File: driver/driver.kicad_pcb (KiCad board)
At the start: 2 copper layers, 100 x 100 mm, 104 parts, among them J1 OUT_A, J2 OUT_B, J3 UART_DEBUG, J4 USB_B_Micro, J5 CH340E module, J6 1602 I2C LCD, J7 IN_VCC, J8 IN_GND, J9 SWD, Q1 TPHR6503PL, Q2 TPHR6503PL, Q3 TPHR6503PL, Q4 TPHR6503PL, SW1 SW_Push, SW2 SW_Push, U1 MT3608, U10 PC817, U2 AMS1117-5.0, U3 AMS1117-3.3, U4 TC4427, U5 TC4427, U6 STM32F103C8Tx, U7 INA226, U8 MCP9804_MSOP, U9 PC817, Y1 8MHz

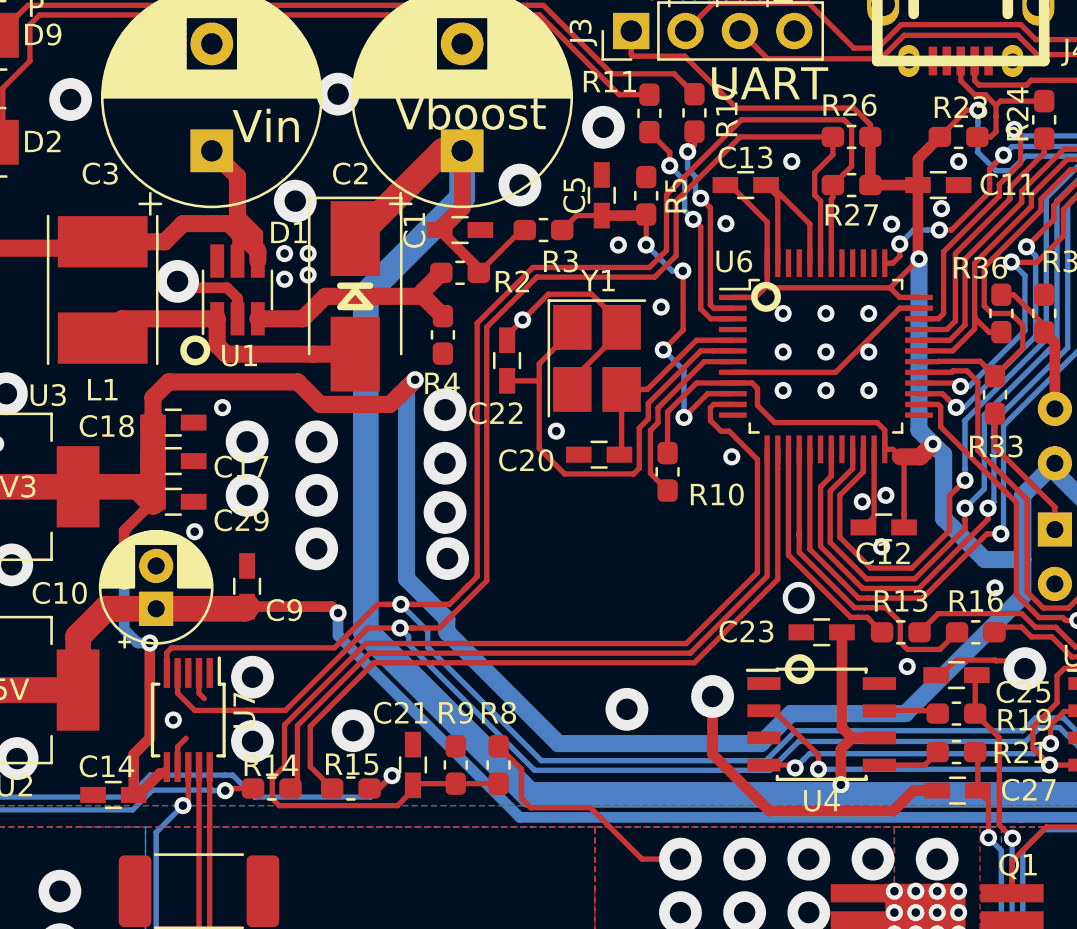
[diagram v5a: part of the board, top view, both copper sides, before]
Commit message: driver: Fatten a few power traces
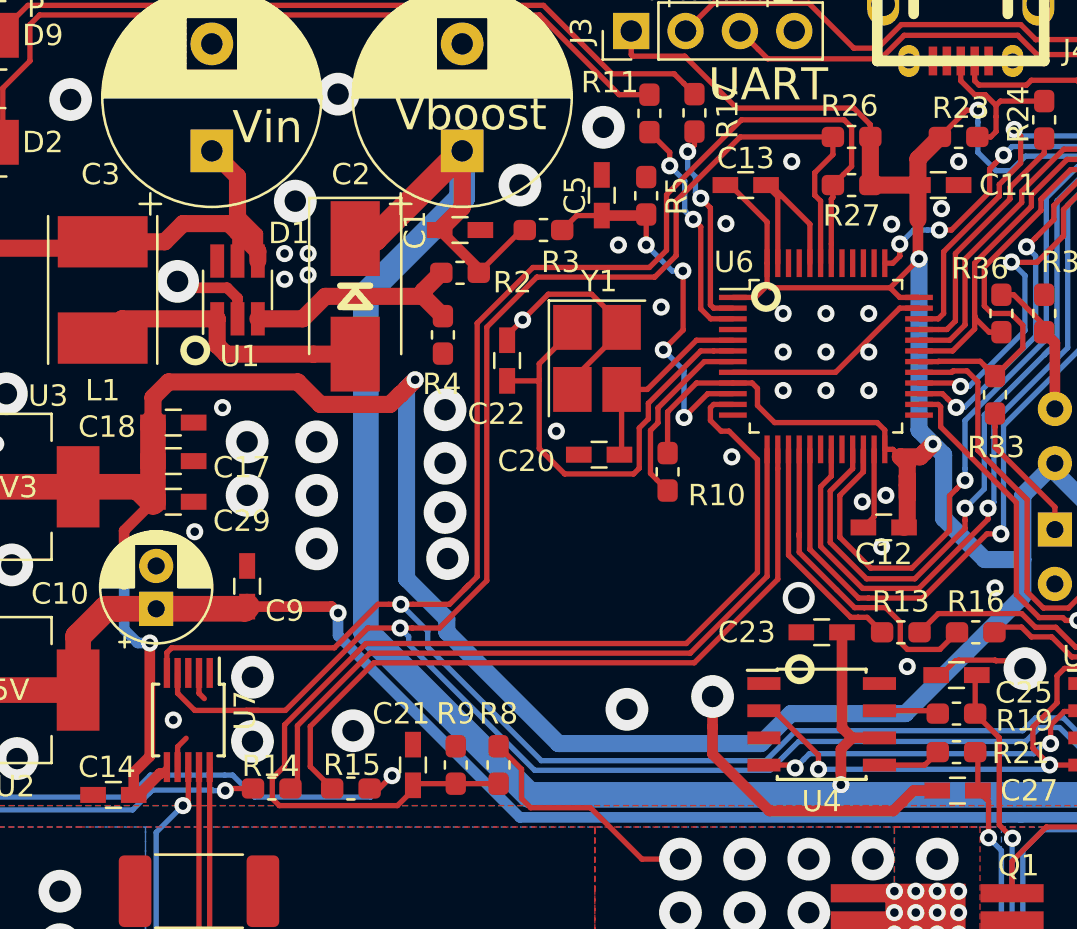
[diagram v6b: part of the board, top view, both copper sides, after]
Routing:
- net +3V3: track 327.3 -> 329.8 mm
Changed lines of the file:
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@@
     (thickness 1.6)
     (drawings 126)
-    (tracks 1371)
+    (tracks 1376)
     (zones 0)
     (modules 104)
@@
     (arrow2b (pts (xy 58 138) (xy 57.413579 136.873496)))
   )
-  (segment (start 107.8 63.4) (end 106.9 63.4) (width 1.2) (layer F.Cu) (net 1))
-  (segment (start 106.9 63.4) (end 104.9 65.4) (width 1.2) (layer F.Cu) (net 1))
-  (segment (start 104.9 65.4) (end 102.8 67.5) (width 1.2) (layer F.Cu) (net 1))
   (segment (start 108.575 69.1) (end 108.575 68.925) (width 0.5) (layer F.Cu) (net 1))
   (segment (start 140.45 93.375) (end 140.45 94.25) (width 0.5) (layer F.Cu) (net 1))
@@
   (segment (start 107.8 66.05) (end 106.75 67.1) (width 0.8) (layer F.Cu) (net 1))
   (segment (start 107.8 63.4) (end 107.8 66.05) (width 0.8) (layer F.Cu) (net 1))
+  (segment (start 103.7 67.5) (end 102.8 67.5) (width 1.2) (layer F.Cu) (net 1))
+  (segment (start 107.8 63.4) (end 103.7 67.5) (width 1.2) (layer F.Cu) (net 1))
   (via (at 80.75 66) (size 2) (drill 1) (layers F.Cu B.Cu) (net 2))
   (via (at 89.5 61) (size 2) (drill 1) (layers F.Cu B.Cu) (net 2))
@@
   (segment (start 111.825 70.1) (end 113.85 70.1) (width 0.25) (layer F.Cu) (net 2))
   (via (at 117.1 70.7) (size 0.8) (drill 0.4) (layers F.Cu B.Cu) (net 2))
-  (via (at 120.4 77.7) (size 0.8) (drill 0.4) (layers F.Cu B.Cu) (net 2))
   (via (at 115.1 67.8) (size 0.8) (drill 0.4) (layers F.Cu B.Cu) (net 2))
   (via (at 123.2 63.9) (size 0.8) (drill 0.4) (layers F.Cu B.Cu) (net 2))
@@
   (via (at 127.869667 66.826237) (size 0.8) (drill 0.4) (layers F.Cu B.Cu) (net 2))
   (via (at 131 63.9) (size 0.8) (drill 0.4) (layers F.Cu B.Cu) (net 2))
+  (via (at 120.4 77.7) (size 0.8) (drill 0.4) (layers F.Cu B.Cu) (net 2))
   (segment (start 97.3 66.32) (end 97.3 65.5) (width 0.5) (layer F.Cu) (net 3))
   (segment (start 98.25 68.55) (end 98.25 67.27) (width 0.5) (layer F.Cu) (net 3))
@@
   (segment (start 89.85 79.1) (end 92.65 79.1) (width 1.2) (layer F.Cu) (net 6))
   (segment (start 94 92.2) (end 94 91.65) (width 0.25) (layer F.Cu) (net 6))
-  (segment (start 126.875 62.75) (end 126.875 65) (width 0.5) (layer F.Cu) (net 6))
   (segment (start 120.325 65) (end 120.1 65) (width 0.25) (layer F.Cu) (net 6))
   (segment (start 122.05 66.725) (end 120.325 65) (width 0.25) (layer F.Cu) (net 6))
@@
   (segment (start 121.5 70.25) (end 122.05 69.7) (width 0.25) (layer F.Cu) (net 6))
   (segment (start 128.45 80.375) (end 128.45 81) (width 0.25) (layer F.Cu) (net 6))
-  (segment (start 128.45 77.875) (end 128.45 80.375) (width 0.25) (layer F.Cu) (net 6))
   (segment (start 127.55 77.35) (end 127.925 77.35) (width 0.25) (layer F.Cu) (net 6))
   (segment (start 127.55 76.45) (end 127.2 76.1) (width 0.25) (layer F.Cu) (net 6))
@@
   (segment (start 120.45 74.25) (end 118.75 74.25) (width 0.25) (layer F.Cu) (net 6))
   (segment (start 118.75 74.25) (end 117.4 75.6) (width 0.25) (layer F.Cu) (net 6))
-  (segment (start 92.45 91.6) (end 92.45 93.5) (width 0.5) (layer F.Cu) (net 6))
-  (segment (start 93.2 90.85) (end 92.45 91.6) (width 0.5) (layer F.Cu) (net 6))
-  (segment (start 92.675 93.5) (end 93.675 92.5) (width 0.5) (layer F.Cu) (net 6))
-  (segment (start 93.675 92.5) (end 93.7 92.5) (width 0.5) (layer F.Cu) (net 6))
-  (segment (start 92.45 93.5) (end 92.675 93.5) (width 0.5) (layer F.Cu) (net 6))
   (segment (start 93.7 92.5) (end 94 92.2) (width 0.25) (layer F.Cu) (net 6))
   (segment (start 93.35 74.925) (end 94.075 74.2) (width 0.8) (layer F.Cu) (net 6))
@@
   (segment (start 135.5 78) (end 134 79.5) (width 0.8) (layer B.Cu) (net 6))
   (segment (start 134 79.5) (end 134 82.5) (width 0.8) (layer B.Cu) (net 6))
-  (segment (start 128.275 77.7) (end 128.45 77.875) (width 0.25) (layer F.Cu) (net 6))
   (segment (start 127.925 77.35) (end 128.275 77.7) (width 0.25) (layer F.Cu) (net 6))
   (via (at 129.15 68.45) (size 0.8) (drill 0.4) (layers F.Cu B.Cu) (net 6))
-  (segment (start 93.2 90.85) (end 93.2 86.4) (width 0.5) (layer F.Cu) (net 6))
   (via (at 93.2 86.4) (size 0.8) (drill 0.4) (layers F.Cu B.Cu) (net 6))
   (via (at 92 83.5) (size 0.8) (drill 0.4) (layers F.Cu B.Cu) (net 6))
@@
   (segment (start 129.15 76.45) (end 129.8 77.1) (width 0.8) (layer B.Cu) (net 6))
   (segment (start 129.15 68.45) (end 129.15 76.45) (width 0.8) (layer B.Cu) (net 6))
-  (segment (start 126.875 65) (end 129.1 65) (width 0.5) (layer F.Cu) (net 6))
-  (segment (start 129.1 63.775) (end 130.125 62.75) (width 0.5) (layer F.Cu) (net 6))
-  (segment (start 129.1 65) (end 129.1 63.775) (width 0.5) (layer F.Cu) (net 6))
   (segment (start 129.1 68.4) (end 129.15 68.45) (width 0.5) (layer F.Cu) (net 6))
-  (segment (start 129.1 65) (end 129.1 68.4) (width 0.5) (layer F.Cu) (net 6))
   (segment (start 134.12299 63.650012) (end 133.448001 64.325001) (width 0.25) (layer B.Cu) (net 6))
   (segment (start 133.448001 64.325001) (end 132.751999 64.325001) (width 0.25) (layer B.Cu) (net 6))
@@
   (segment (start 152.34 60.2) (end 152.34 61.3) (width 0.25) (layer B.Cu) (net 6))
   (segment (start 130.125 62.75) (end 131.375 61.5) (width 0.25) (layer F.Cu) (net 6))
+  (segment (start 128.600001 79.019999) (end 128.600001 79.6) (width 0.8) (layer F.Cu) (net 6))
+  (segment (start 128.275 77.7) (end 128.600001 78.025001) (width 0.8) (layer F.Cu) (net 6))
+  (segment (start 128.600001 79.6) (end 128.45 80.375) (width 0.25) (layer F.Cu) (net 6))
+  (segment (start 128.600001 78.6) (end 128.600001 80.849999) (width 0.8) (layer F.Cu) (net 6))
+  (segment (start 128.600001 80.849999) (end 128.45 81) (width 0.8) (layer F.Cu) (net 6))
+  (segment (start 128.600001 78.6) (end 128.600001 79.019999) (width 0.8) (layer F.Cu) (net 6))
+  (segment (start 128.600001 78.025001) (end 128.600001 78.6) (width 0.8) (layer F.Cu) (net 6))
+  (segment (start 92.675 93.5) (end 93.675 92.5) (width 0.5) (layer F.Cu) (net 6))
+  (segment (start 92.45 93.5) (end 92.675 93.5) (width 0.5) (layer F.Cu) (net 6))
+  (segment (start 93.675 92.5) (end 93.7 92.5) (width 0.5) (layer F.Cu) (net 6))
+  (segment (start 92.45 92.45) (end 92.45 93.5) (width 0.5) (layer F.Cu) (net 6))
+  (segment (start 93.2 86.4) (end 93.2 91.7) (width 0.5) (layer F.Cu) (net 6))
+  (segment (start 93.2 91.7) (end 92.45 92.45) (width 0.5) (layer F.Cu) (net 6))
+  (segment (start 129.1 65) (end 129.1 66.619998) (width 0.8) (layer F.Cu) (net 6))
+  (segment (start 129.1 66.619998) (end 129.1 68.4) (width 0.5) (layer F.Cu) (net 6))
+  (segment (start 129.1 63.775) (end 130.125 62.75) (width 0.8) (layer F.Cu) (net 6))
+  (segment (start 129.1 65) (end 129.1 63.775) (width 0.8) (layer F.Cu) (net 6))
+  (segment (start 126.875 62.75) (end 126.875 65) (width 0.8) (layer F.Cu) (net 6))
+  (segment (start 126.875 65) (end 129.1 65) (width 0.8) (layer F.Cu) (net 6))
   (segment (start 83.5875 90.9375) (end 83.55 90.9) (width 1.2) (layer F.Cu) (net 7))
   (segment (start 81.6 90.9) (end 83.55 90.9) (width 1.2) (layer F.Cu) (net 7))
@@
   (segment (start 105.575 92.975) (end 105.5 93.05) (width 0.25) (layer F.Cu) (net 9))
   (segment (start 107.5 92.975) (end 105.575 92.975) (width 0.25) (layer F.Cu) (net 9))
-  (segment (start 105.5 93.275) (end 105.5 93.05) (width 0.25) (layer F.Cu) (net 9))
-  (segment (start 120.273002 76.5) (end 121.599989 77.826987) (width 0.25) (layer F.Cu) (net 9))
-  (segment (start 119.55 75.25) (end 119.4 75.4) (width 0.25) (layer F.Cu) (net 9))
-  (segment (start 119.4 75.4) (end 119.4 76) (width 0.25) (layer F.Cu) (net 9))
-  (segment (start 121.599989 77.826987) (end 121.59999 83.100011) (width 0.25) (layer F.Cu) (net 9))
-  (segment (start 121.59999 83.100011) (end 118.274998 86.425003) (width 0.25) (layer F.Cu) (net 9))
+  (segment (start 99.2545 94.00001) (end 104.77499 94.00001) (width 0.25) (layer F.Cu) (net 9))
+  (segment (start 98.92499 93.6705) (end 99.2545 94.00001) (width 0.25) (layer F.Cu) (net 9))
+  (segment (start 98.92499 92.7295) (end 98.92499 93.6705) (width 0.25) (layer F.Cu) (net 9))
   (segment (start 99.5 92.15449) (end 98.92499 92.7295) (width 0.25) (layer F.Cu) (net 9))
-  (segment (start 119.9 76.5) (end 120.273002 76.5) (width 0.25) (layer F.Cu) (net 9))
-  (segment (start 120.45 75.25) (end 119.55 75.25) (width 0.25) (layer F.Cu) (net 9))
-  (segment (start 103.302176 86.425003) (end 99.5 90.227179) (width 0.25) (layer F.Cu) (net 9))
   (segment (start 99.5 90.227179) (end 99.5 92.15449) (width 0.25) (layer F.Cu) (net 9))
+  (segment (start 103.302176 86.425003) (end 99.5 90.227179) (width 0.25) (layer F.Cu) (net 9))
   (segment (start 118.274998 86.425003) (end 103.302176 86.425003) (width 0.25) (layer F.Cu) (net 9))
-  (segment (start 98.92499 92.7295) (end 98.92499 93.6705) (width 0.25) (layer F.Cu) (net 9))
-  (segment (start 98.92499 93.6705) (end 99.2545 94.00001) (width 0.25) (layer F.Cu) (net 9))
+  (segment (start 121.599989 77.826987) (end 121.59999 83.100011) (width 0.25) (layer F.Cu) (net 9))
+  (segment (start 119.55 75.25) (end 119.4 75.4) (width 0.25) (layer F.Cu) (net 9))
+  (segment (start 120.45 75.25) (end 119.55 75.25) (width 0.25) (layer F.Cu) (net 9))
   (segment (start 119.4 76) (end 119.9 76.5) (width 0.25) (layer F.Cu) (net 9))
-  (segment (start 99.2545 94.00001) (end 104.77499 94.00001) (width 0.25) (layer F.Cu) (net 9))
+  (segment (start 121.59999 83.100011) (end 118.274998 86.425003) (width 0.25) (layer F.Cu) (net 9))
+  (segment (start 119.4 75.4) (end 119.4 76) (width 0.25) (layer F.Cu) (net 9))
+  (segment (start 119.9 76.5) (end 120.273002 76.5) (width 0.25) (layer F.Cu) (net 9))
   (segment (start 104.77499 94.00001) (end 105.5 93.275) (width 0.25) (layer F.Cu) (net 9))
+  (segment (start 120.273002 76.5) (end 121.599989 77.826987) (width 0.25) (layer F.Cu) (net 9))
+  (segment (start 105.5 93.275) (end 105.5 93.05) (width 0.25) (layer F.Cu) (net 9))
   (segment (start 112.95 71.8) (end 112.95 71.65) (width 0.25) (layer F.Cu) (net 10))
   (segment (start 111.4 73.35) (end 112.95 71.8) (width 0.25) (layer F.Cu) (net 10))
